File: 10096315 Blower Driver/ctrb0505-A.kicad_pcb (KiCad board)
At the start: 4 copper layers, 92.5 x 72 mm, 310 parts, among them IC1 L-BC-SO24, IC2 L-BC-SO08, IC3 L-BC-SO08, IC4 L-BC-SO08, IC5 L-BC-SO08, IC6 REG-BC-DPAK, J1 F-COCMS-MOL43650-0212, J11 F-CO-MOL5566-02, J2 F-CO-HE10-2010D, J22 F-CO-MOL7395M09, J3 F-CO-MOL7395M02, J6 F-CO-MOL7395M08, T1 Q-SOT23-IRLML2803, T10 Q-SOT23-IRLML2803, T2 Q-BC-DPAK-GDS, T3 Q-BC-DPAK-GDS, T4 Q-BC-DPAK-GDS, T5 Q-BC-DPAK-GDS, T6 Q-BC-DPAK-GDS, T7 Q-BC-DPAK-GDS, T8 Q-SOT23-IRLML2803, T9 Q-BC-DPAK-GDS

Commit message: Blower do some symbol libraries and restart pcb from scratch w new version
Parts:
- removed ? (x167): , 
- removed cam1: COIN_EXTERNE, ctrb0505-A1_clean.PcbLib:cam1
- removed cam12: FABRICATION-FEE, ctrb0505-A1_clean.PcbLib:cam12
- removed cam13: PERCAGE_TABLEAU, ctrb0505-A1_clean.PcbLib:cam13
- removed cam14: FEE_COMP, ctrb0505-A1_clean.PcbLib:cam14
- removed cam15: FEE_COMP, ctrb0505-A1_clean.PcbLib:cam15
- removed cam2: COIN_EXTERNE, ctrb0505-A1_clean.PcbLib:cam2
- removed cam3: COIN_EXTERNE, ctrb0505-A1_clean.PcbLib:cam3
- removed cam4: COIN_EXTERNE, ctrb0505-A1_clean.PcbLib:cam4
- removed cam5: FILM18_HORIZONTAL, ctrb0505-A1_clean.PcbLib:cam5
- removed cam6: A3_PER_COVIDIEN, ctrb0505-A1_clean.PcbLib:cam6
- removed cam7: A3_EQFC_COVIDIEN, ctrb0505-A1_clean.PcbLib:cam7
- removed cam8: PER-COVIDIEN_TEXTE, ctrb0505-A1_clean.PcbLib:cam8
- removed cam9: A3_EQFS_COVIDIEN, ctrb0505-A1_clean.PcbLib:cam9
- added CAM1: COIN_EXTERNE, ctrb0505-A:COIN_EXTERNE_1, F.Cu at (241.4, 34.6)
- added CAM12: FABRICATION-FEE, ctrb0505-A:FABRICATION-FEE_1, F.Cu at (139.1, 0.01)
- added CAM13: PERCAGE_TABLEAU, ctrb0505-A:PERCAGE_TABLEAU_1, F.Cu at (130.2, 82.7)
- added CAM14: FEE_COMP, ctrb0505-A:FEE_COMP_2, B.Cu at (247.2, 105.6)
- added CAM15: FEE_COMP, ctrb0505-A:FEE_COMP_1, F.Cu at (315.1, 105.6)
- added CAM2: COIN_EXTERNE, ctrb0505-A:COIN_EXTERNE_1, F.Cu at (241.4, 106.6)
- added CAM3: COIN_EXTERNE, ctrb0505-A:COIN_EXTERNE_1, F.Cu at (334.0, 106.6)
- added CAM4: COIN_EXTERNE, ctrb0505-A:COIN_EXTERNE_1, F.Cu at (334.0, 34.6)
- added CAM5: FILM18_HORIZONTAL, ctrb0505-A:FILM18_HORIZONTAL_1, F.Cu at (288.5, 76.6)
- added CAM6: A3_PER_COVIDIEN, ctrb0505-A:A3_PER_COVIDIEN_1, F.Cu at (206.1, 96.0)
- added CAM7: A3_EQFC_COVIDIEN, ctrb0505-A:A3_EQFC_COVIDIEN_1, F.Cu at (287.0, 89.6)
- added CAM8: PER-COVIDIEN_TEXTE, ctrb0505-A:PER-COVIDIEN_TEXTE_1, F.Cu at (250.9, 137.6)
- added CAM9: A3_EQFS_COVIDIEN, ctrb0505-A:A3_EQFS_COVIDIEN_1, B.Cu at (287.4, 72.6)
- added J4: JUMPER2_NoCopper, ctrb0505-A:JUMPER2_NoCopper_1, F.Cu at (246.5, 60.6)
- added L1: ELC09DxxxxF_NoCopper, ctrb0505-A:ELC09DxxxxF_NoCopper_1, F.Cu at (251.6, 60.6)
- added TH1: , ctrb0505-A:ThroughHole_36milx12mil_Pad_Cu_Mask, F.Cu at (295.2, 54.0)
- added TH2: , ctrb0505-A:ThroughHole_36milx12mil_Pad_Cu_Mask, F.Cu at (291.7, 54.5)
- added TH3: , ctrb0505-A:ThroughHole_36milx12mil_Pad_Cu_Mask, F.Cu at (290.6, 71.2)
- added TH4: , ctrb0505-A:ThroughHole_36milx12mil_Pad_Cu_Mask, F.Cu at (278.8, 71.2)
- added TH5: , ctrb0505-A:ThroughHole_36milx12mil_Pad_Cu_Mask, F.Cu at (266.7, 71.2)
- added TH6: , ctrb0505-A:ThroughHole_36milx12mil_Pad_Cu_Mask, F.Cu at (266.2, 51.9)
- C1: footprint ctrb0505-A1_clean.PcbLib:C1 -> ctrb0505-A:C0805_1
- C10: footprint ctrb0505-A1_clean.PcbLib:C10 -> ctrb0505-A:RC1206_1
- C11: footprint ctrb0505-A1_clean.PcbLib:C11 -> ctrb0505-A:C0603_1
- C12: footprint ctrb0505-A1_clean.PcbLib:C12 -> ctrb0505-A:C0805_1
- C13: footprint ctrb0505-A1_clean.PcbLib:C13 -> ctrb0505-A:RC1206_1
- C14: footprint ctrb0505-A1_clean.PcbLib:C14 -> ctrb0505-A:C0603_1
- C15: footprint ctrb0505-A1_clean.PcbLib:C15 -> ctrb0505-A:C0805_1
- C16: footprint ctrb0505-A1_clean.PcbLib:C16 -> ctrb0505-A:RC1206_1
- C17: footprint ctrb0505-A1_clean.PcbLib:C17 -> ctrb0505-A:C0603_1
- C18: footprint ctrb0505-A1_clean.PcbLib:C18 -> ctrb0505-A:C0805_1
- C19: footprint ctrb0505-A1_clean.PcbLib:C19 -> ctrb0505-A:C0805_1
- C2: footprint ctrb0505-A1_clean.PcbLib:C2 -> ctrb0505-A:03515_1
- C20: footprint ctrb0505-A1_clean.PcbLib:C20 -> ctrb0505-A:C0603_1
- C21: footprint ctrb0505-A1_clean.PcbLib:C21 -> ctrb0505-A:C0805_1
- C22: footprint ctrb0505-A1_clean.PcbLib:C22 -> ctrb0505-A:C0612-4_1
- C23: footprint ctrb0505-A1_clean.PcbLib:C23 -> ctrb0505-A:C0612-4_1
- C24: footprint ctrb0505-A1_clean.PcbLib:C24 -> ctrb0505-A:C0805_1
- C25: footprint ctrb0505-A1_clean.PcbLib:C25 -> ctrb0505-A:C0805_1
- C26: footprint ctrb0505-A1_clean.PcbLib:C26 -> ctrb0505-A:C0805_1
- C27: footprint ctrb0505-A1_clean.PcbLib:C27 -> ctrb0505-A:03515_1
- C28: footprint ctrb0505-A1_clean.PcbLib:C28 -> ctrb0505-A:HT-13X27_1
- C29: footprint ctrb0505-A1_clean.PcbLib:C29 -> ctrb0505-A:HT-13X27_1
- C3: footprint ctrb0505-A1_clean.PcbLib:C3 -> ctrb0505-A:C0805_1
- C4: footprint ctrb0505-A1_clean.PcbLib:C4 -> ctrb0505-A:C7343_1
- C5: footprint ctrb0505-A1_clean.PcbLib:C5 -> ctrb0505-A:C0805_1
- C6: footprint ctrb0505-A1_clean.PcbLib:C6 -> ctrb0505-A:C0805_1
- C7: footprint ctrb0505-A1_clean.PcbLib:C7 -> ctrb0505-A:C0603_1
- C8: footprint ctrb0505-A1_clean.PcbLib:C8 -> ctrb0505-A:C0603_1
- C9: footprint ctrb0505-A1_clean.PcbLib:C9 -> ctrb0505-A:C0805_1
- D1: footprint ctrb0505-A1_clean.PcbLib:D1 -> ctrb0505-A:SMB_1
- D10: footprint ctrb0505-A1_clean.PcbLib:D10 -> ctrb0505-A:SMA_1
- D11: footprint ctrb0505-A1_clean.PcbLib:D11 -> ctrb0505-A:SOD80_1
- D12: footprint ctrb0505-A1_clean.PcbLib:D12 -> ctrb0505-A:SOD80_1
- D13: footprint ctrb0505-A1_clean.PcbLib:D13 -> ctrb0505-A:SOD80_1
- D14: footprint ctrb0505-A1_clean.PcbLib:D14 -> ctrb0505-A:SOT23-1G_1
- D15: footprint ctrb0505-A1_clean.PcbLib:D15 -> ctrb0505-A:SOT23-1G_1
- D16: footprint ctrb0505-A1_clean.PcbLib:D16 -> ctrb0505-A:SOT23-1G_1
- D17: footprint ctrb0505-A1_clean.PcbLib:D17 -> ctrb0505-A:DPAK-2ANODES_1
- D18: footprint ctrb0505-A1_clean.PcbLib:D18 -> ctrb0505-A:SMB_1
- D19: footprint ctrb0505-A1_clean.PcbLib:D19 -> ctrb0505-A:SMB_1
- D2: footprint ctrb0505-A1_clean.PcbLib:D2 -> ctrb0505-A:SOD323_1
- D20: footprint ctrb0505-A1_clean.PcbLib:D20 -> ctrb0505-A:SMB_1
- D21: footprint ctrb0505-A1_clean.PcbLib:D21 -> ctrb0505-A:SMB_1
- D22: footprint ctrb0505-A1_clean.PcbLib:D22 -> ctrb0505-A:SMB_1
- D23: footprint ctrb0505-A1_clean.PcbLib:D23 -> ctrb0505-A:SMB_1
- D24: footprint ctrb0505-A1_clean.PcbLib:D24 -> ctrb0505-A:SOT23-1G_1
- D3: footprint ctrb0505-A1_clean.PcbLib:D3 -> ctrb0505-A:SOD323_1
- D4: footprint ctrb0505-A1_clean.PcbLib:D4 -> ctrb0505-A:SOD323_1
- D5: footprint ctrb0505-A1_clean.PcbLib:D5 -> ctrb0505-A:SOD323_1
- D6: footprint ctrb0505-A1_clean.PcbLib:D6 -> ctrb0505-A:SOD323_1
- D7: footprint ctrb0505-A1_clean.PcbLib:D7 -> ctrb0505-A:SOD323_1
- D8: footprint ctrb0505-A1_clean.PcbLib:D8 -> ctrb0505-A:SMA_1
- D9: footprint ctrb0505-A1_clean.PcbLib:D9 -> ctrb0505-A:SMA_1
- F1: footprint ctrb0505-A1_clean.PcbLib:F1 -> ctrb0505-A:FU154000_1
- FI1: footprint ctrb0505-A1_clean.PcbLib:FI1 -> ctrb0505-A:BNX002_1
- FI3: footprint ctrb0505-A1_clean.PcbLib:FI3 -> ctrb0505-A:C0603_1
- FI4: footprint ctrb0505-A1_clean.PcbLib:FI4 -> ctrb0505-A:C0603_1
- FI5: footprint ctrb0505-A1_clean.PcbLib:FI5 -> ctrb0505-A:C0603_1
- FI6: footprint ctrb0505-A1_clean.PcbLib:FI6 -> ctrb0505-A:C0603_1
- FI7: footprint ctrb0505-A1_clean.PcbLib:FI7 -> ctrb0505-A:C0603_1
- FI8: footprint ctrb0505-A1_clean.PcbLib:FI8 -> ctrb0505-A:C0603_1
- FI9: footprint ctrb0505-A1_clean.PcbLib:FI9 -> ctrb0505-A:C0603_1
- IC1: footprint ctrb0505-A1_clean.PcbLib:IC1 -> ctrb0505-A:MX.A24_COMPOSANT_1
- IC2: footprint ctrb0505-A1_clean.PcbLib:IC2 -> ctrb0505-A:MX.A8_COMPOSANT_1
- IC3: footprint ctrb0505-A1_clean.PcbLib:IC3 -> ctrb0505-A:MX.A8_COMPOSANT_1
- IC4: footprint ctrb0505-A1_clean.PcbLib:IC4 -> ctrb0505-A:MX.A8_COMPOSANT_1
- IC5: footprint ctrb0505-A1_clean.PcbLib:IC5 -> ctrb0505-A:MX.A8_COMPOSANT_1
- IC6: footprint ctrb0505-A1_clean.PcbLib:IC6 -> ctrb0505-A:DPAK_1
- J1: footprint ctrb0505-A1_clean.PcbLib:J1 -> ctrb0505-A:MOL43650-02C_1
- J11: footprint ctrb0505-A1_clean.PcbLib:J11 -> ctrb0505-A:MOL5566-2_1
- J2: footprint ctrb0505-A1_clean.PcbLib:J2 -> ctrb0505-A:BP2X5D_1
- J22: footprint ctrb0505-A1_clean.PcbLib:J22 -> ctrb0505-A:MOL7395-9_1
- J3: footprint ctrb0505-A1_clean.PcbLib:J3 -> ctrb0505-A:MOL7395-2_1
- J6: footprint ctrb0505-A1_clean.PcbLib:J6 -> ctrb0505-A:MOL7395-8_1
- MIR1: footprint ctrb0505-A1_clean.PcbLib:MIR1 -> ctrb0505-A:MIRECMS-SAFT_1
- MIR2: footprint ctrb0505-A1_clean.PcbLib:MIR2 -> ctrb0505-A:MIRECMS-SAFT_1
- MIR3: footprint ctrb0505-A1_clean.PcbLib:MIR3 -> ctrb0505-A:MIRECMS-SAFT_1
- MIR4: footprint ctrb0505-A1_clean.PcbLib:MIR4 -> ctrb0505-A:MIRECMS-SAFT_1
- PT1: footprint ctrb0505-A1_clean.PcbLib:PT1 -> ctrb0505-A:C12000_1
- R1: footprint ctrb0505-A1_clean.PcbLib:R1 -> ctrb0505-A:R2512_1
- R10: footprint ctrb0505-A1_clean.PcbLib:R10 -> ctrb0505-A:R0603_1
- R11: footprint ctrb0505-A1_clean.PcbLib:R11 -> ctrb0505-A:R0603_1
- R12: footprint ctrb0505-A1_clean.PcbLib:R12 -> ctrb0505-A:R0603_1
- R13: footprint ctrb0505-A1_clean.PcbLib:R13 -> ctrb0505-A:R0603_1
- R2: footprint ctrb0505-A1_clean.PcbLib:R2 -> ctrb0505-A:R0603_1
- R20: footprint ctrb0505-A1_clean.PcbLib:R20 -> ctrb0505-A:R0603_1
- R3: footprint ctrb0505-A1_clean.PcbLib:R3 -> ctrb0505-A:R0603_1
- R30: footprint ctrb0505-A1_clean.PcbLib:R30 -> ctrb0505-A:R0603_1
- R31: footprint ctrb0505-A1_clean.PcbLib:R31 -> ctrb0505-A:R0603_1
- R32: footprint ctrb0505-A1_clean.PcbLib:R32 -> ctrb0505-A:R0603_1
- R33: footprint ctrb0505-A1_clean.PcbLib:R33 -> ctrb0505-A:R0603_1
- R35: footprint ctrb0505-A1_clean.PcbLib:R35 -> ctrb0505-A:R0603_1
- R37: footprint ctrb0505-A1_clean.PcbLib:R37 -> ctrb0505-A:R0603_1
- R38: footprint ctrb0505-A1_clean.PcbLib:R38 -> ctrb0505-A:R0603_1
- R39: footprint ctrb0505-A1_clean.PcbLib:R39 -> ctrb0505-A:R0603_1
- R4: footprint ctrb0505-A1_clean.PcbLib:R4 -> ctrb0505-A:R0603_1
- R40: footprint ctrb0505-A1_clean.PcbLib:R40 -> ctrb0505-A:R2512_1
- R41: footprint ctrb0505-A1_clean.PcbLib:R41 -> ctrb0505-A:R0603_1
- R42: footprint ctrb0505-A1_clean.PcbLib:R42 -> ctrb0505-A:R0603_1
- R5: footprint ctrb0505-A1_clean.PcbLib:R5 -> ctrb0505-A:R0603_1
- R50: footprint ctrb0505-A1_clean.PcbLib:R50 -> ctrb0505-A:R0603_1
- R58: footprint ctrb0505-A1_clean.PcbLib:R58 -> ctrb0505-A:RC1206_1
- R59: footprint ctrb0505-A1_clean.PcbLib:R59 -> ctrb0505-A:RC1206_1
- R6: footprint ctrb0505-A1_clean.PcbLib:R6 -> ctrb0505-A:R0603_1
- R60: footprint ctrb0505-A1_clean.PcbLib:R60 -> ctrb0505-A:RC1206_1
- R7: footprint ctrb0505-A1_clean.PcbLib:R7 -> ctrb0505-A:R0603_1
- R8: footprint ctrb0505-A1_clean.PcbLib:R8 -> ctrb0505-A:R0603_1
- R9: footprint ctrb0505-A1_clean.PcbLib:R9 -> ctrb0505-A:R0603_1
- T1: footprint ctrb0505-A1_clean.PcbLib:T1 -> ctrb0505-A:SOT23-GSD_1
- T10: footprint ctrb0505-A1_clean.PcbLib:T10 -> ctrb0505-A:SOT23-GSD_1
- T2: footprint ctrb0505-A1_clean.PcbLib:T2 -> ctrb0505-A:DPAK-GDS_1
- T3: footprint ctrb0505-A1_clean.PcbLib:T3 -> ctrb0505-A:DPAK-GDS_1
- T4: footprint ctrb0505-A1_clean.PcbLib:T4 -> ctrb0505-A:DPAK-GDS_1
- T5: footprint ctrb0505-A1_clean.PcbLib:T5 -> ctrb0505-A:DPAK-GDS_1
- T6: footprint ctrb0505-A1_clean.PcbLib:T6 -> ctrb0505-A:DPAK-GDS_1
- T7: footprint ctrb0505-A1_clean.PcbLib:T7 -> ctrb0505-A:DPAK-GDS_1
- T8: footprint ctrb0505-A1_clean.PcbLib:T8 -> ctrb0505-A:SOT23-GSD_1
- T9: footprint ctrb0505-A1_clean.PcbLib:T9 -> ctrb0505-A:DPAK-GDS_1
- ZC2: footprint ctrb0505-A1_clean.PcbLib:ZC21 -> ctrb0505-A:C-SC8_1
- ZC27: footprint ctrb0505-A1_clean.PcbLib:ZC22 -> ctrb0505-A:C-SC10_1
- ZM1: footprint ctrb0505-A1_clean.PcbLib:ZM1 -> ctrb0505-A:FIX35M_1
- ZM2: footprint ctrb0505-A1_clean.PcbLib:ZM2 -> ctrb0505-A:FIX35M_1
- ZM3: footprint ctrb0505-A1_clean.PcbLib:ZM3 -> ctrb0505-A:FIX35M_1
- ZM4: footprint ctrb0505-A1_clean.PcbLib:ZM4 -> ctrb0505-A:FIX35M_1
- ZT2: footprint ctrb0505-A1_clean.PcbLib:ZT2 -> ctrb0505-A:TO220ABGDS-INV_COUCHE_1
- ZT3: footprint ctrb0505-A1_clean.PcbLib:ZT3 -> ctrb0505-A:TO220ABGDS-INV_COUCHE_1
- ZT4: footprint ctrb0505-A1_clean.PcbLib:ZT4 -> ctrb0505-A:TO220ABGDS-INV_COUCHE_1
- ZT5: footprint ctrb0505-A1_clean.PcbLib:ZT5 -> ctrb0505-A:TO220ABGDS-INV_COUCHE_1
- ZT6: footprint ctrb0505-A1_clean.PcbLib:ZT6 -> ctrb0505-A:TO220ABGDS-INV_COUCHE_1
- ZT7: footprint ctrb0505-A1_clean.PcbLib:ZT7 -> ctrb0505-A:TO220ABGDS-INV_COUCHE_1
- moved C28 235.8 mm to (268.0, 54.1)
- moved C29 235.8 mm to (268.0, 41.1)
- moved J1 235.8 mm to (261.5, 54.3)
- moved C3 235.8 mm to (299.2, 58.7)
- moved D24 235.8 mm to (285.9, 63.1)
- moved FI1 235.8 mm to (249.1, 60.6)
- moved IC6 235.8 mm to (292.9, 44.7), turned to 0 degrees
- moved MIR1 235.8 mm to (244.0, 37.1)
- moved R11 235.8 mm to (267.5, 94.9)
- moved R12 235.8 mm to (279.5, 94.9)
- moved R13 235.8 mm to (291.6, 94.9)
- moved R40 235.8 mm to (305.6, 72.6)
- moved R7 235.8 mm to (329.7, 72.6)
- moved T10 235.8 mm to (282.1, 63.1)
- moved C10 235.8 mm to (271.9, 98.0)
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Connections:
- net BRAKE/ renamed BRAKE_
- net FAULT/ renamed FAULT_
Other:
- net class All Nets removed
- rule pad_to_mask_clearance: 0.05 -> 0.051
- board text removed: "(1)Fabrique suivant IPC A610 classe III. (1)Manufactured according to IPC A610 class III."
- board text removed: "0,3"
- board text removed: "0,8"
- board text removed: "0,9"
- board text removed: "0,95"
- board text removed: "1,2"
- board text removed: "1,4"
- board text removed: "3,5"
- board text removed: "35u"
- board text removed: "A"
- board text removed: "ATTENTION: Le circuit imprime doit etre UL94V-0. (2)Le fabricant doit etre reconnu UL et doit apposer le marquage correspondant."
- board text removed: "BLANCHE"
- board text removed: "Cote de pliage des TO220"
- board text removed: "Dimension folding of TO220"
- board text removed: "Fabrique suivant IPC A610 classe III. Manufactured according to IPC A610 class III."
- board text removed: "J4"
- board text removed: "L1"
- board text removed: "NOTA: C2 et C27 sont montes en double implantation.r Two assemblies possible for C2 and C27"
- board text removed: "NOTA: T2 a T7 montes en double implantation. r Plaquer les composants T2 a T7 r lorsqu'ils sont montes en boitier TO220 afin d'obtenir une coplaneite optimum."
- board text removed: "T2"
- board text removed: "T7"
- board text removed: "The printed circuit board must be UL94V-0 (2) The manufacturer must be recognized UL and must affix corresponding marking."
- board text removed: "Toutes les dimensions sonr en millimetres. All the dimensions are in millimeter."
- board text removed: "Two assemblies possible from T2 to T7.r To plate the T2 components in T7 r when they are assembled out of caseTO220 r in order to obtain an optimum co planarity."
- board text removed: "VERT"
- board text removed: "X"
- board text removed: "YES"

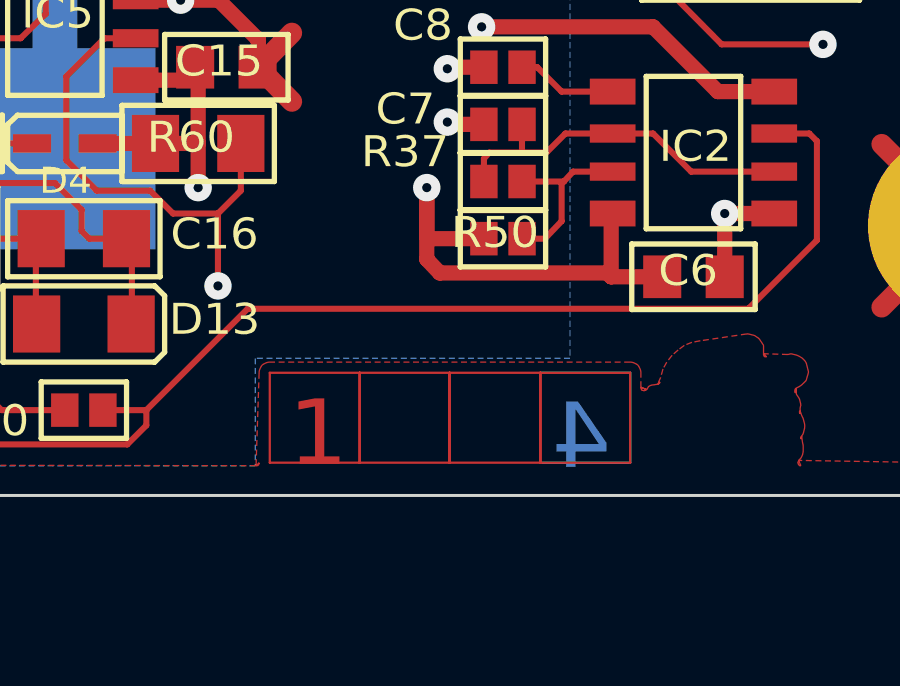
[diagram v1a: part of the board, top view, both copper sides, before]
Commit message: Layout Kicad: remove DRC due to text zone definition
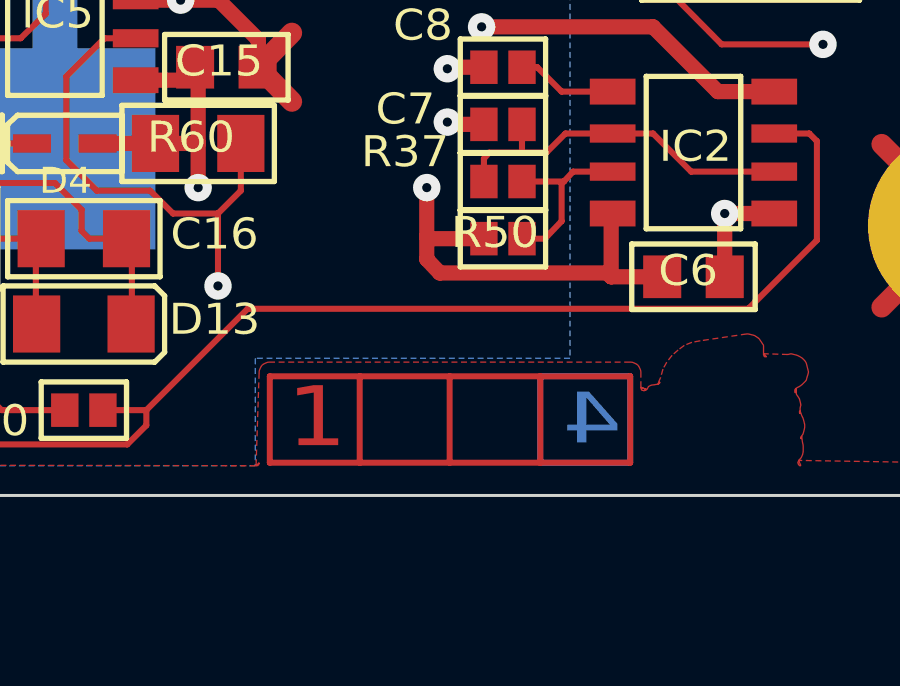
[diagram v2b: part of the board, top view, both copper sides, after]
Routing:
- net (no net): track 84.0 -> 73.6 mm
- net +15V: track 166.5 -> 164.9 mm
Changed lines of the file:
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@@
-(kicad_pcb (version 20171130) (host pcbnew 5.1.5-52549c5~86~ubuntu18.04.1)
+(kicad_pcb (version 20171130) (host pcbnew 5.1.5+dfsg1-2build2)
   (general
     (thickness 1.6)
     (drawings 63)
-    (tracks 1113)
+    (tracks 1110)
     (zones 0)
     (modules 151)
@@
     (1 In1.Cu signal hide)
     (2 In2.Cu signal hide)
-    (31 B.Cu signal hide)
+    (31 B.Cu signal)
     (32 B.Adhes user)
     (33 F.Adhes user)
@@
   (setup
     (last_trace_width 0.25)
+    (user_trace_width 0.508)
     (trace_clearance 0.2)
     (zone_clearance 0.508)
@@
     (solder_mask_min_width 0.25)
     (aux_axis_origin 0 0)
-    (visible_elements FFFFFF7F)
+    (visible_elements FFFEFF7F)
     (pcbplotparams
       (layerselection 0x010fc_ffffffff)
@@
       (net 39 N10))
   )
-  (gr_text 1 (at 302.557 105.801) (layer F.Cu)
-    (effects (font (size 2.182774 2.295906) (thickness 0.0762)) (justify left bottom))
+  (gr_text 1 (at 302.514 105.156) (layer F.Cu)
+    (effects (font (size 2 2.295906) (thickness 0.2)) (justify left bottom))
   )
-  (gr_text 4 (at 313.3266 105.9026) (layer B.Cu)
-    (effects (font (size 2.182774 2.295906) (thickness 0.0762)) (justify left bottom mirror))
+  (gr_text 4 (at 313.69 105.029) (layer B.Cu)
+    (effects (font (size 1.7 2.295906) (thickness 0.2)) (justify left bottom mirror))
   )
   (gr_line (start 241.4446 106.5884) (end 333.9514 106.5884) (layer Edge.Cuts) (width 0.1))
@@
     (effects (font (size 1.73289 1.822704) (thickness 0.0762)) (justify left bottom mirror))
   )
-  (gr_text 2 (at 305.5542 105.801) (layer In1.Cu)
-    (effects (font (size 2.182774 2.295906) (thickness 0.0762)) (justify left bottom))
+  (gr_text 2 (at 305.435 105.156) (layer In1.Cu)
+    (effects (font (size 2 2.295906) (thickness 0.2)) (justify left bottom))
   )
-  (gr_text 3 (at 310.3294 105.801) (layer In2.Cu)
-    (effects (font (size 2.182774 2.295906) (thickness 0.0762)) (justify left bottom mirror))
+  (gr_text 3 (at 310.388 105.156) (layer In2.Cu)
+    (effects (font (size 2 2.295906) (thickness 0.2)) (justify left bottom mirror))
   )
-  (segment (start 304.9446 105.4962) (end 307.9418 105.4962) (width 0.0762) (layer F.Cu) (net 0))
-  (segment (start 307.9418 105.4962) (end 307.9418 102.499) (width 0.0762) (layer F.Cu) (net 0))
-  (segment (start 304.9446 102.499) (end 307.9418 102.499) (width 0.0762) (layer F.Cu) (net 0))
-  (segment (start 304.9446 105.4962) (end 304.9446 102.499) (width 0.0762) (layer F.Cu) (net 0))
-  (segment (start 301.9474 105.4962) (end 304.9446 105.4962) (width 0.0762) (layer F.Cu) (net 0))
-  (segment (start 304.9446 105.4962) (end 304.9446 102.499) (width 0.0762) (layer F.Cu) (net 0))
-  (segment (start 301.9474 102.499) (end 304.9446 102.499) (width 0.0762) (layer F.Cu) (net 0))
-  (segment (start 301.9474 105.4962) (end 301.9474 102.499) (width 0.0762) (layer F.Cu) (net 0))
-  (segment (start 307.9418 105.4962) (end 310.9644 105.4962) (width 0.0762) (layer F.Cu) (net 0))
-  (segment (start 310.9644 105.4962) (end 310.9644 102.499) (width 0.0762) (layer F.Cu) (net 0))
-  (segment (start 307.9418 102.499) (end 310.9644 102.499) (width 0.0762) (layer F.Cu) (net 0))
-  (segment (start 307.9418 105.4962) (end 307.9418 102.499) (width 0.0762) (layer F.Cu) (net 0))
-  (segment (start 310.9644 105.4962) (end 313.9616 105.4962) (width 0.0762) (layer F.Cu) (net 0))
-  (segment (start 313.9616 105.4962) (end 313.9616 102.499) (width 0.0762) (layer F.Cu) (net 0))
-  (segment (start 310.9644 102.499) (end 313.9616 102.499) (width 0.0762) (layer F.Cu) (net 0))
-  (segment (start 310.9644 105.4962) (end 310.9644 102.499) (width 0.0762) (layer F.Cu) (net 0))
-  (segment (start 310.9644 105.4962) (end 313.9616 105.4962) (width 0.0762) (layer B.Cu) (net 0))
-  (segment (start 313.9616 105.4962) (end 313.9616 102.499) (width 0.0762) (layer B.Cu) (net 0))
-  (segment (start 310.9644 102.499) (end 313.9616 102.499) (width 0.0762) (layer B.Cu) (net 0))
-  (segment (start 310.9644 105.4962) (end 310.9644 102.499) (width 0.0762) (layer B.Cu) (net 0))
-  (segment (start 304.9446 105.4962) (end 307.9418 105.4962) (width 0.0762) (layer In1.Cu) (net 0))
-  (segment (start 307.9418 105.4962) (end 307.9418 102.499) (width 0.0762) (layer In1.Cu) (net 0))
-  (segment (start 304.9446 102.499) (end 307.9418 102.499) (width 0.0762) (layer In1.Cu) (net 0))
-  (segment (start 304.9446 105.4962) (end 304.9446 102.499) (width 0.0762) (layer In1.Cu) (net 0))
-  (segment (start 307.9418 105.4962) (end 310.9644 105.4962) (width 0.0762) (layer In2.Cu) (net 0))
-  (segment (start 310.9644 105.4962) (end 310.9644 102.499) (width 0.0762) (layer In2.Cu) (net 0))
-  (segment (start 307.9418 102.499) (end 310.9644 102.499) (width 0.0762) (layer In2.Cu) (net 0))
-  (segment (start 307.9418 105.4962) (end 307.9418 102.499) (width 0.0762) (layer In2.Cu) (net 0))
+  (segment (start 304.9446 105.4962) (end 307.9418 105.4962) (width 0.2) (layer F.Cu) (net 0))
+  (segment (start 304.9446 102.616) (end 307.9418 102.616) (width 0.2) (layer F.Cu) (net 0))
+  (segment (start 301.9474 105.4962) (end 304.9446 105.4962) (width 0.2) (layer F.Cu) (net 0))
+  (segment (start 304.9446 105.4962) (end 304.9446 102.616) (width 0.2) (layer F.Cu) (net 0))
+  (segment (start 301.9474 102.616) (end 304.9446 102.616) (width 0.2) (layer F.Cu) (net 0))
+  (segment (start 301.9474 105.4962) (end 301.9474 102.616) (width 0.2) (layer F.Cu) (net 0))
+  (segment (start 307.9418 105.4962) (end 310.9644 105.4962) (width 0.2) (layer F.Cu) (net 0))
+  (segment (start 307.9418 102.616) (end 310.9644 102.616) (width 0.2) (layer F.Cu) (net 0))
+  (segment (start 307.9418 105.4962) (end 307.9418 102.616) (width 0.2) (layer F.Cu) (net 0))
+  (segment (start 310.9644 105.4962) (end 313.9616 105.4962) (width 0.2) (layer F.Cu) (net 0))
+  (segment (start 313.9616 105.4962) (end 313.9616 102.616) (width 0.2) (layer F.Cu) (net 0))
+  (segment (start 310.9644 102.616) (end 313.9616 102.616) (width 0.2) (layer F.Cu) (net 0))
+  (segment (start 310.9644 105.4962) (end 310.9644 102.616) (width 0.2) (layer F.Cu) (net 0))
+  (segment (start 310.9468 105.4962) (end 313.944 105.4962) (width 0.2) (layer B.Cu) (net 0))
+  (segment (start 313.9616 105.4962) (end 313.9616 102.616) (width 0.2) (layer B.Cu) (net 0))
+  (segment (start 310.9644 102.616) (end 313.9616 102.616) (width 0.2) (layer B.Cu) (net 0))
+  (segment (start 310.9644 105.4962) (end 310.9644 102.616) (width 0.2) (layer B.Cu) (net 0))
+  (segment (start 304.9446 105.4962) (end 307.9418 105.4962) (width 0.2) (layer In1.Cu) (net 0))
+  (segment (start 307.9418 105.4962) (end 307.9418 102.616) (width 0.2) (layer In1.Cu) (net 0))
+  (segment (start 304.9446 102.616) (end 307.9418 102.616) (width 0.2) (layer In1.Cu) (net 0))
+  (segment (start 304.9446 105.4962) (end 304.9446 102.616) (width 0.2) (layer In1.Cu) (net 0))
+  (segment (start 307.9418 105.4962) (end 310.9644 105.4962) (width 0.2) (layer In2.Cu) (net 0))
+  (segment (start 310.9644 105.41) (end 310.9644 102.616) (width 0.2) (layer In2.Cu) (net 0))
+  (segment (start 307.9418 102.616) (end 310.9644 102.616) (width 0.2) (layer In2.Cu) (net 0))
+  (segment (start 307.9418 105.41) (end 307.9418 102.616) (width 0.2) (layer In2.Cu) (net 0))
   (segment (start 312.6408 50.048) (end 313.9616 51.3434) (width 0.2032) (layer F.Cu) (net 1))
   (segment (start 312.6408 50.048) (end 312.6408 45.5522) (width 0.2032) (layer F.Cu) (net 1))
@@
   (segment (start 296.4356 65.1356) (end 297.1214 64.4752) (width 0.9906) (layer F.Cu) (net 52))
   (segment (start 297.1214 64.4752) (end 299.2296 64.4752) (width 0.9906) (layer F.Cu) (net 52))
-  (segment (start 307.1798 98.7144) (end 307.1798 96.3268) (width 0.508) (layer F.Cu) (net 52))
   (segment (start 307.1798 98.7144) (end 307.6116 99.1716) (width 0.508) (layer F.Cu) (net 52))
   (segment (start 307.6116 99.1716) (end 313.1996 99.1716) (width 0.508) (layer F.Cu) (net 52))
@@
   (segment (start 305.9098 70.0886) (end 305.9098 67.2184) (width 0.9906) (layer In2.Cu) (net 52))
   (segment (start 309.0086 90.9674) (end 309.0086 80.2486) (width 0.9906) (layer In2.Cu) (net 52))
+  (segment (start 307.1798 98.7144) (end 307.1798 97.9524) (width 0.508) (layer F.Cu) (net 52))
   (via (at 311.4216 46.6698) (size 0.9144) (drill 0.3048) (layers F.Cu B.Cu) (net 53))
   (via (at 317.3398 44.0536) (size 0.9144) (drill 0.3048) (layers F.Cu B.Cu) (net 53))

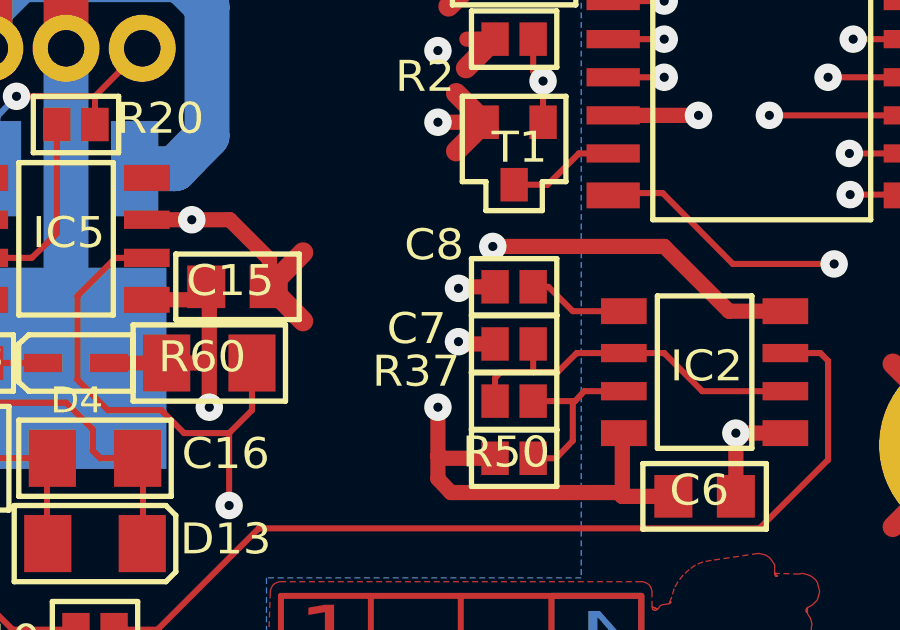
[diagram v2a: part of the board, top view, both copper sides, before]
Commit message: Layout Kicad: remove DRC due to small distance between gnd vias and +15V in layer 2
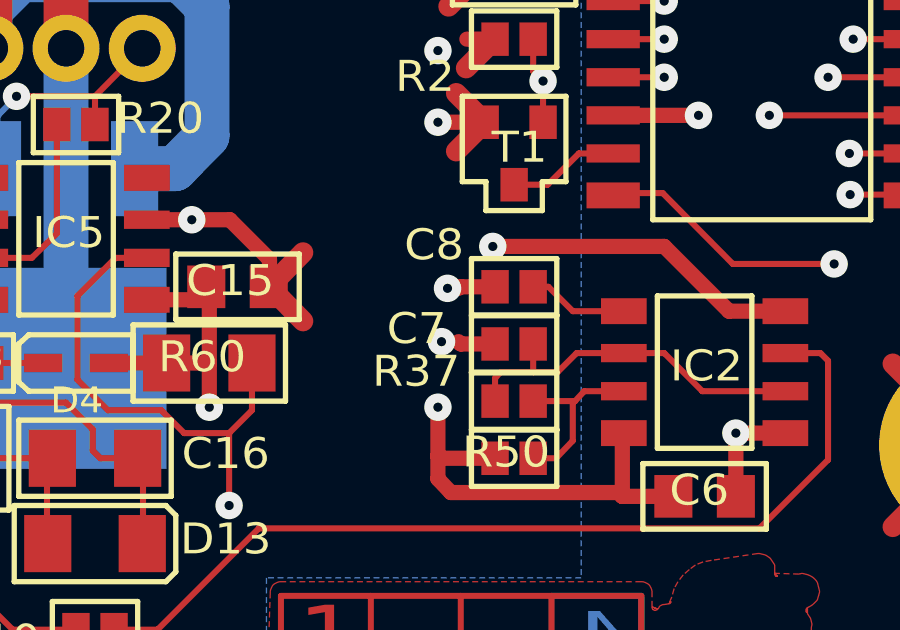
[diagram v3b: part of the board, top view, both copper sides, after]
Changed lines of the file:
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@@
     (0 F.Cu signal hide)
     (1 In1.Cu signal hide)
-    (2 In2.Cu signal hide)
-    (31 B.Cu signal)
+    (2 In2.Cu signal)
+    (31 B.Cu signal hide)
     (32 B.Adhes user)
     (33 F.Adhes user)
@@
   (via (at 329.2778 87.3098) (size 0.9144) (drill 0.3048) (layers F.Cu B.Cu) (net 55))
   (via (at 298.9756 90.0784) (size 0.9144) (drill 0.3048) (layers F.Cu B.Cu) (net 55))
-  (via (at 307.8656 92.3644) (size 0.9144) (drill 0.3048) (layers F.Cu B.Cu) (net 55))
-  (via (at 307.8656 94.1424) (size 0.9144) (drill 0.3048) (layers F.Cu B.Cu) (net 55))
+  (via (at 307.5 92.3644) (size 0.9144) (drill 0.3048) (layers F.Cu B.Cu) (net 55))
+  (via (at 307.3 94.1424) (size 0.9144) (drill 0.3048) (layers F.Cu B.Cu) (net 55))
   (via (at 317.1112 97.1904) (size 0.9144) (drill 0.3048) (layers F.Cu B.Cu) (net 55))
   (via (at 287.0376 90.0784) (size 0.9144) (drill 0.3048) (layers F.Cu B.Cu) (net 55))
